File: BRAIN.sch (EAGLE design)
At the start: 60 parts, among them IC1 ATMEGA328P, IC2 EUP3476SO08T, IC3 RXB1, IC4 TX-C1FLAT, J1 DC_2_1MM, Q1 RJU003N03 N-MOSFET, Q2 RJU003N03 N-MOSFET, Q3 RJU003N03 N-MOSFET, X1 16MHz HC49S

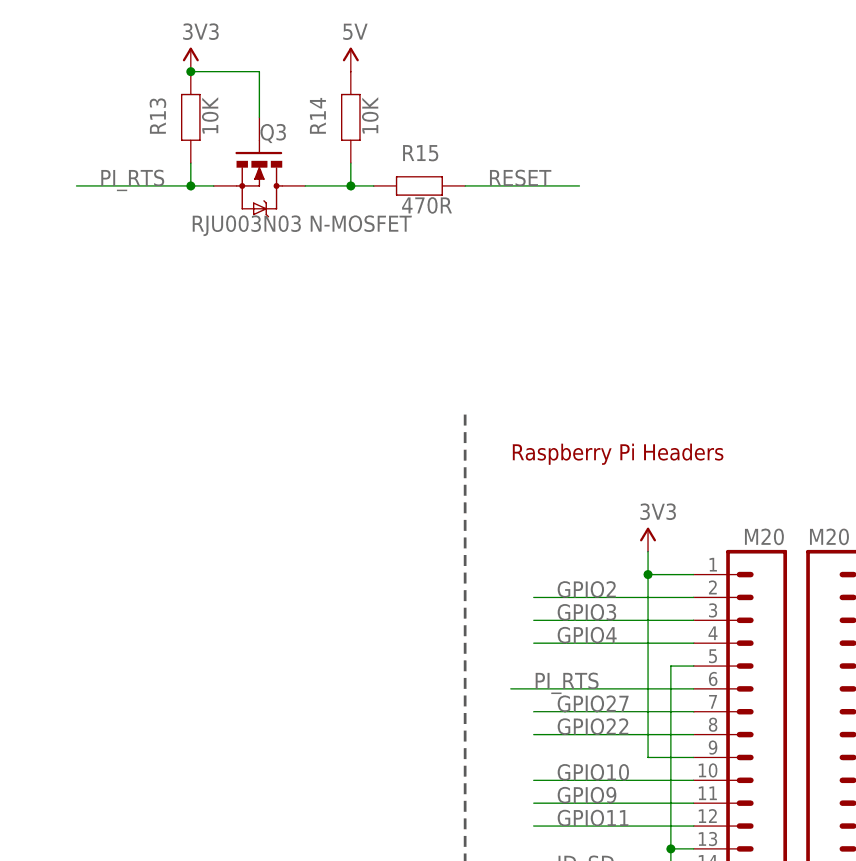
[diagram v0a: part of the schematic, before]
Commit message: Moved Arduino RESET line from RTS to GPIO4 for manual control
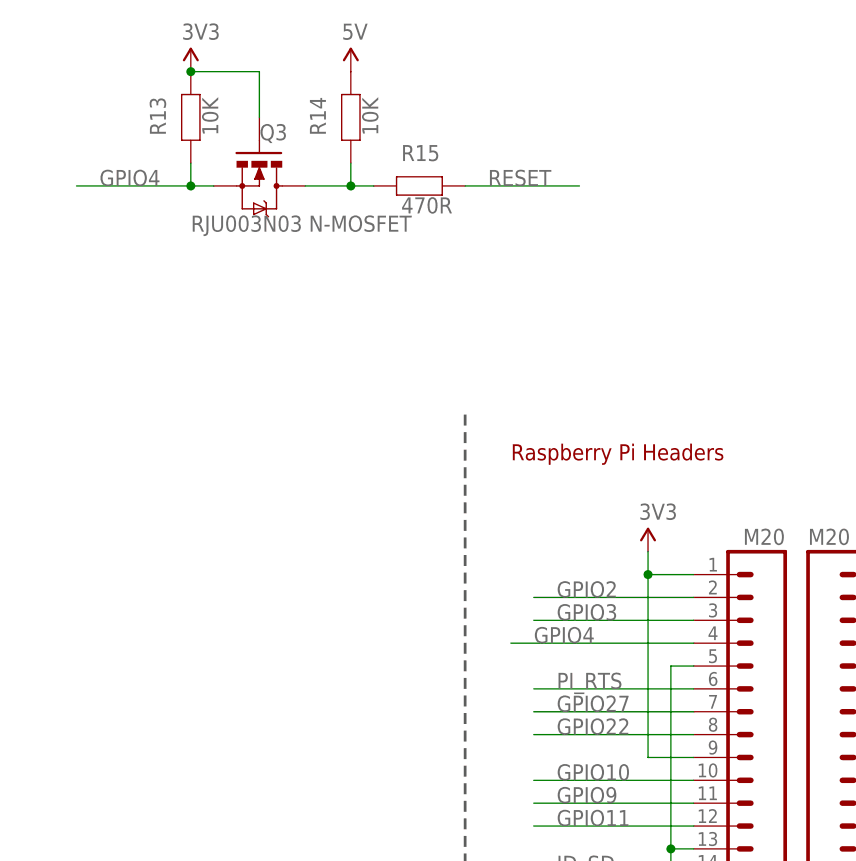
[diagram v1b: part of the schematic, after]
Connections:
- net GPIO4: now also Q3.S, R13.2
- net PI_RTS: no longer Q3.S, R13.2
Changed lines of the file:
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@@
 <net name="PI_RTS" class="0">
 <segment>
-<pinref part="Q3" gate="G$1" pin="S"/>
-<wire x1="10.16" y1="205.74" x2="22.86" y2="205.74" width="0.1524" layer="91"/>
-<pinref part="R13" gate="G$1" pin="2"/>
-<wire x1="22.86" y1="205.74" x2="25.4" y2="205.74" width="0.1524" layer="91"/>
-<wire x1="22.86" y1="208.28" x2="22.86" y2="205.74" width="0.1524" layer="91"/>
-<junction x="22.86" y="205.74"/>
-<label x="12.7" y="205.74" size="1.778" layer="95"/>
-</segment>
-<segment>
 <pinref part="H1" gate="G$1" pin="6"/>
-<wire x1="78.74" y1="149.86" x2="58.42" y2="149.86" width="0.1524" layer="91"/>
-<label x="60.96" y="149.86" size="1.778" layer="95"/>
+<wire x1="78.74" y1="149.86" x2="60.96" y2="149.86" width="0.1524" layer="91"/>
+<label x="63.5" y="149.86" size="1.778" layer="95"/>
 </segment>
 </net>
@@
 <segment>
 <pinref part="H1" gate="G$1" pin="4"/>
-<wire x1="78.74" y1="154.94" x2="60.96" y2="154.94" width="0.1524" layer="91"/>
-<label x="63.5" y="154.94" size="1.778" layer="95"/>
+<wire x1="78.74" y1="154.94" x2="58.42" y2="154.94" width="0.1524" layer="91"/>
+<label x="60.96" y="154.94" size="1.778" layer="95"/>
+</segment>
+<segment>
+<pinref part="Q3" gate="G$1" pin="S"/>
+<wire x1="10.16" y1="205.74" x2="22.86" y2="205.74" width="0.1524" layer="91"/>
+<pinref part="R13" gate="G$1" pin="2"/>
+<wire x1="22.86" y1="205.74" x2="25.4" y2="205.74" width="0.1524" layer="91"/>
+<wire x1="22.86" y1="208.28" x2="22.86" y2="205.74" width="0.1524" layer="91"/>
+<junction x="22.86" y="205.74"/>
+<label x="12.7" y="205.74" size="1.778" layer="95"/>
 </segment>
 </net>

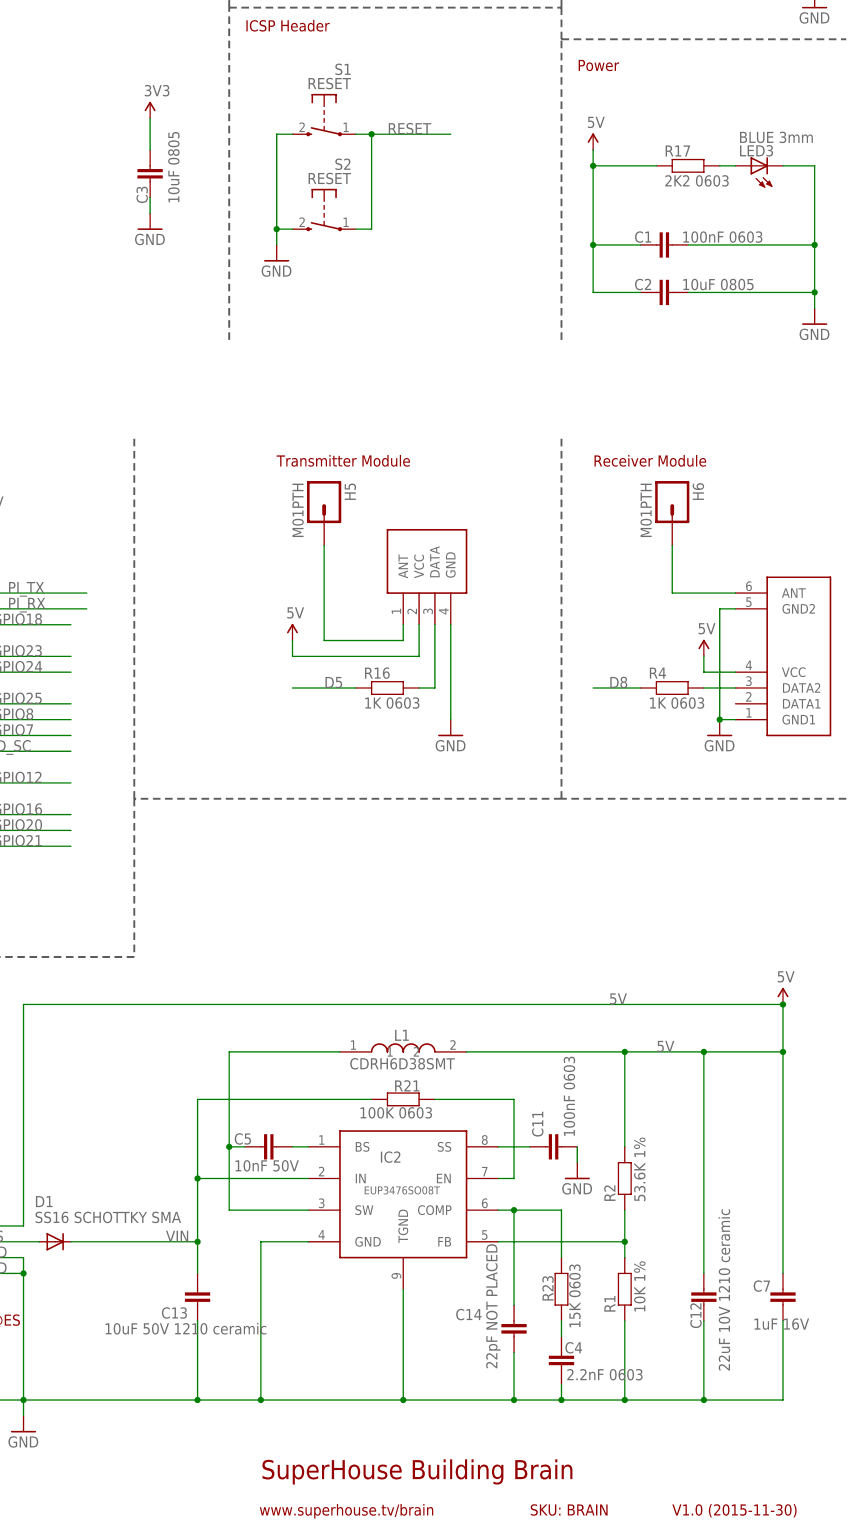
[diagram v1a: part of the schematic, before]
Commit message: Replaced 0805 footprints with 1210
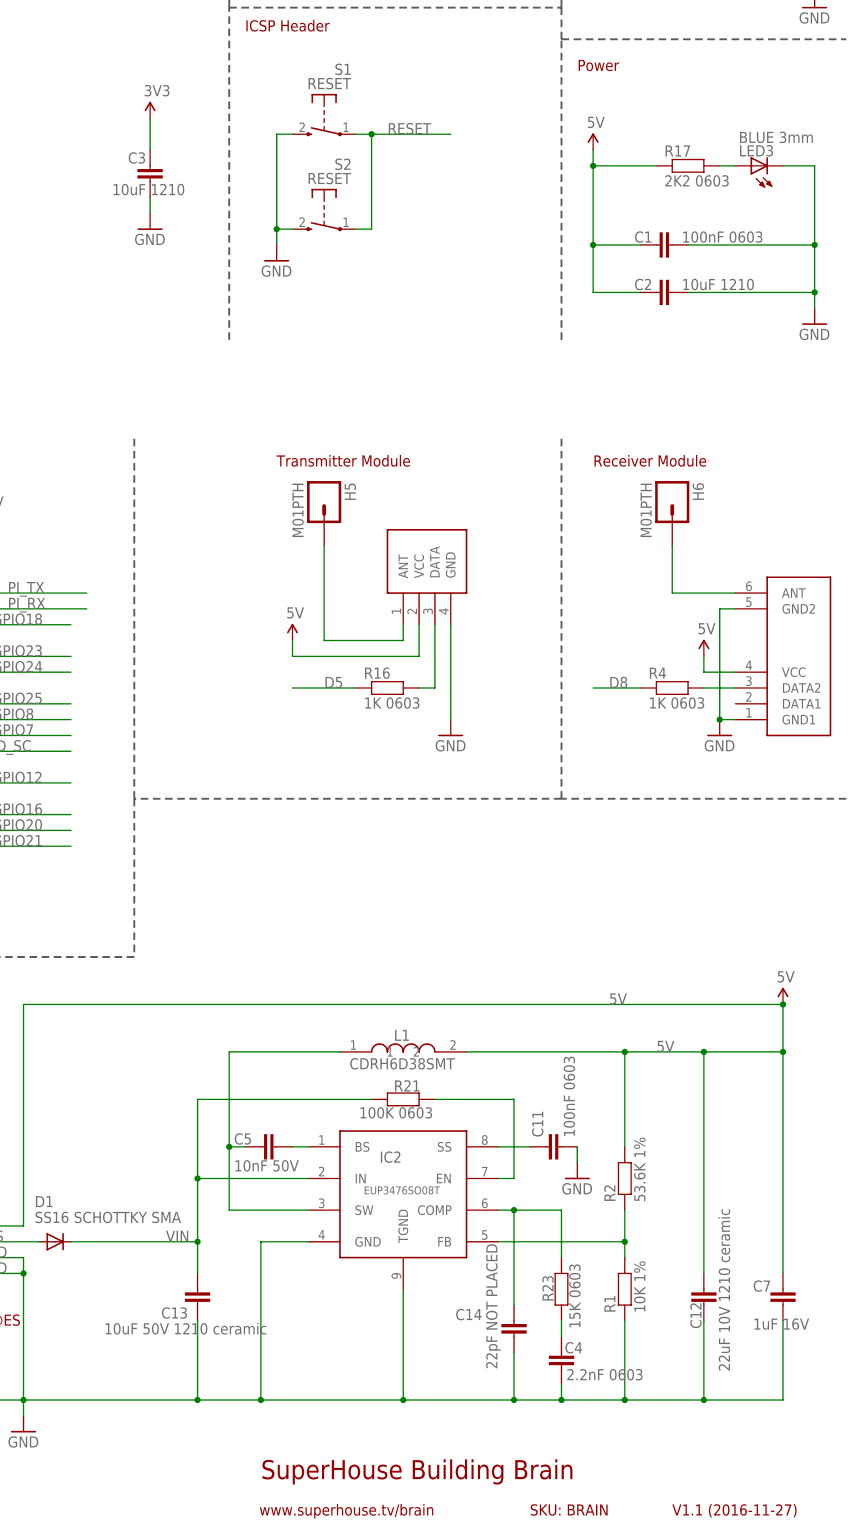
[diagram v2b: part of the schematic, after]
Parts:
- C2, C3: value 10uF 0805 -> 10uF 1210; device freetronics-jon:C-EUC0805 -> freetronics-jon:C-EUC1210
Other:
- note added: "V1.1 (2016-11-27)"
- note removed: "V1.0 (2015-11-30)"
- moved on the sheet: C2
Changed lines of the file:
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@@
 <part name="H5" library="freetronics" deviceset="M01" device="PTH"/>
 <part name="U$6" library="SparkFun" deviceset="5V" device=""/>
-<part name="C2" library="freetronics-jon" deviceset="C-EU" device="C0805" value="10uF 0805"/>
 <part name="GND5" library="SparkFun" deviceset="GND" device=""/>
 <part name="IC1" library="freetronics-master-v1.1" deviceset="AVR-MEGA8" device="-AI" value="ATMEGA328P"/>
@@
 <part name="S2" library="freetronics-jon" deviceset="TAC_SWITCH_2PIN" device="" value="RESET"/>
 <part name="GND10" library="SparkFun" deviceset="GND" device=""/>
-<part name="C3" library="freetronics-jon" deviceset="C-EU" device="C0805" value="10uF 0805"/>
+<part name="C3" library="freetronics-jon" deviceset="C-EU" device="C1210" value="10uF 1210"/>
+<part name="C2" library="freetronics-jon" deviceset="C-EU" device="C1210" value="10uF 1210"/>
 </parts>
 <sheets>
@@
 <text x="149.86" y="12.7" size="3.048" layer="94">SuperHouse Building Brain</text>
 <text x="193.04" y="6.858" size="1.778" layer="94">SKU: BRAIN</text>
-<text x="215.9" y="6.858" size="1.778" layer="94">V1.0 (2015-11-30)</text>
+<text x="215.9" y="6.858" size="1.778" layer="94">V1.1 (2016-11-27)</text>
 <text x="200.66" y="238.76" size="1.778" layer="94">Power</text>
 <text x="203.2" y="175.26" size="1.778" layer="94">Receiver Module</text>
@@
 <instance part="H5" gate="G$1" x="160.02" y="170.18" rot="R270"/>
 <instance part="U$6" gate="G$1" x="154.94" y="147.32"/>
-<instance part="C2" gate="G$1" x="215.9" y="203.2" smashed="yes" rot="R270">
-<attribute name="NAME" x="209.804" y="203.581" size="1.778" layer="95"/>
-<attribute name="VALUE" x="217.424" y="203.581" size="1.778" layer="96"/>
-</instance>
 <instance part="GND5" gate="1" x="132.08" y="342.9"/>
 <instance part="IC1" gate="G$1" x="193.04" y="322.58"/>
@@
 <instance part="S2" gate="1" x="160.02" y="213.36" rot="MR0"/>
 <instance part="GND10" gate="1" x="152.4" y="208.28"/>
-<instance part="C3" gate="G$1" x="132.08" y="223.52" smashed="yes">
-<attribute name="NAME" x="131.699" y="217.424" size="1.778" layer="95" rot="R90"/>
-<attribute name="VALUE" x="136.779" y="217.424" size="1.778" layer="96" rot="R90"/>
+<instance part="C3" gate="G$1" x="132.08" y="223.52" smashed="yes" rot="MR0">
+<attribute name="NAME" x="128.524" y="225.679" size="1.778" layer="95" rot="MR180"/>
+<attribute name="VALUE" x="125.984" y="220.599" size="1.778" layer="96" rot="MR180"/>
+</instance>
+<instance part="C2" gate="G$1" x="215.9" y="203.2" smashed="yes" rot="MR90">
+<attribute name="NAME" x="209.804" y="205.359" size="1.778" layer="95" rot="MR180"/>
+<attribute name="VALUE" x="217.424" y="205.359" size="1.778" layer="96" rot="MR180"/>
 </instance>
 </instances>
@@
 <wire x1="213.36" y1="223.52" x2="203.2" y2="223.52" width="0.1524" layer="91"/>
 <junction x="203.2" y="223.52"/>
-<pinref part="C2" gate="G$1" pin="2"/>
 <wire x1="210.82" y1="203.2" x2="203.2" y2="203.2" width="0.1524" layer="91"/>
 <wire x1="203.2" y1="203.2" x2="203.2" y2="210.82" width="0.1524" layer="91"/>
 <junction x="203.2" y="210.82"/>
 <pinref part="R17" gate="G$1" pin="1"/>
+<pinref part="C2" gate="G$1" pin="2"/>
 </segment>
 <segment>
@@
 <pinref part="GND1" gate="1" pin="GND"/>
 <wire x1="233.68" y1="223.52" x2="238.76" y2="223.52" width="0.1524" layer="91"/>
-<pinref part="C2" gate="G$1" pin="1"/>
 <wire x1="218.44" y1="203.2" x2="238.76" y2="203.2" width="0.1524" layer="91"/>
 <junction x="238.76" y="203.2"/>
 <pinref part="LED3" gate="G$1" pin="C"/>
-</segment>
-<segment>
+<pinref part="C2" gate="G$1" pin="1"/>
+</segment>
+<segment>

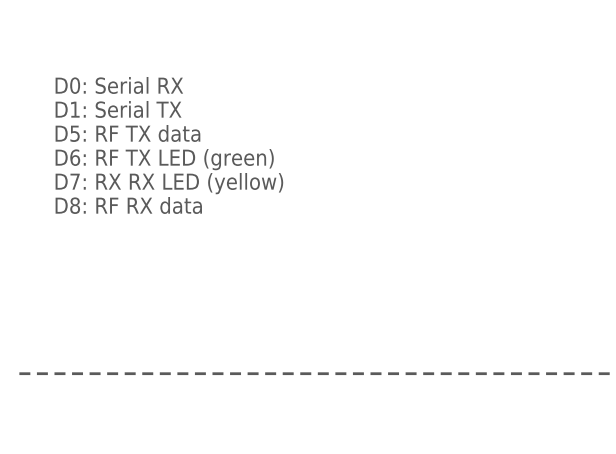
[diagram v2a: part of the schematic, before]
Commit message: Improved designators
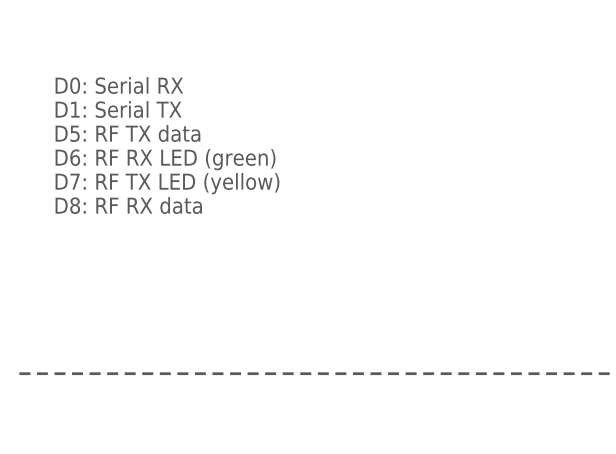
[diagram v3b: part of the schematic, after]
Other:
- note added: "D0: Serial RX D1: Serial TX D5: RF TX data D6: RF RX LED (green) D7: RF TX LED (yellow) D8: RF RX data"
- note removed: "D0: Serial RX D1: Serial TX D5: RF TX data D6: RF TX LED (green) D7: RX RX LED (yellow) D8: RF RX data"
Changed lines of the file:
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@@
 D1: Serial TX
 D5: RF TX data
-D6: RF TX LED (green)
-D7: RX RX LED (yellow)
+D6: RF RX LED (green)
+D7: RF TX LED (yellow)
 D8: RF RX data</text>
 <wire x1="3.81" y1="332.74" x2="109.22" y2="332.74" width="0.3048" layer="97" style="longdash"/>
